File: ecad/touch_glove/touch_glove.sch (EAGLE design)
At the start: 175 parts, among them Q1 MCH3474 4A/30V, Q2 MCH3474 4A/30V, Q3 MCH3474 4A/30V, Q4 MCH3474 4A/30V, Q5 MCH3474 4A/30V, Q6 MCH3474 4A/30V, SW1 4A/28V

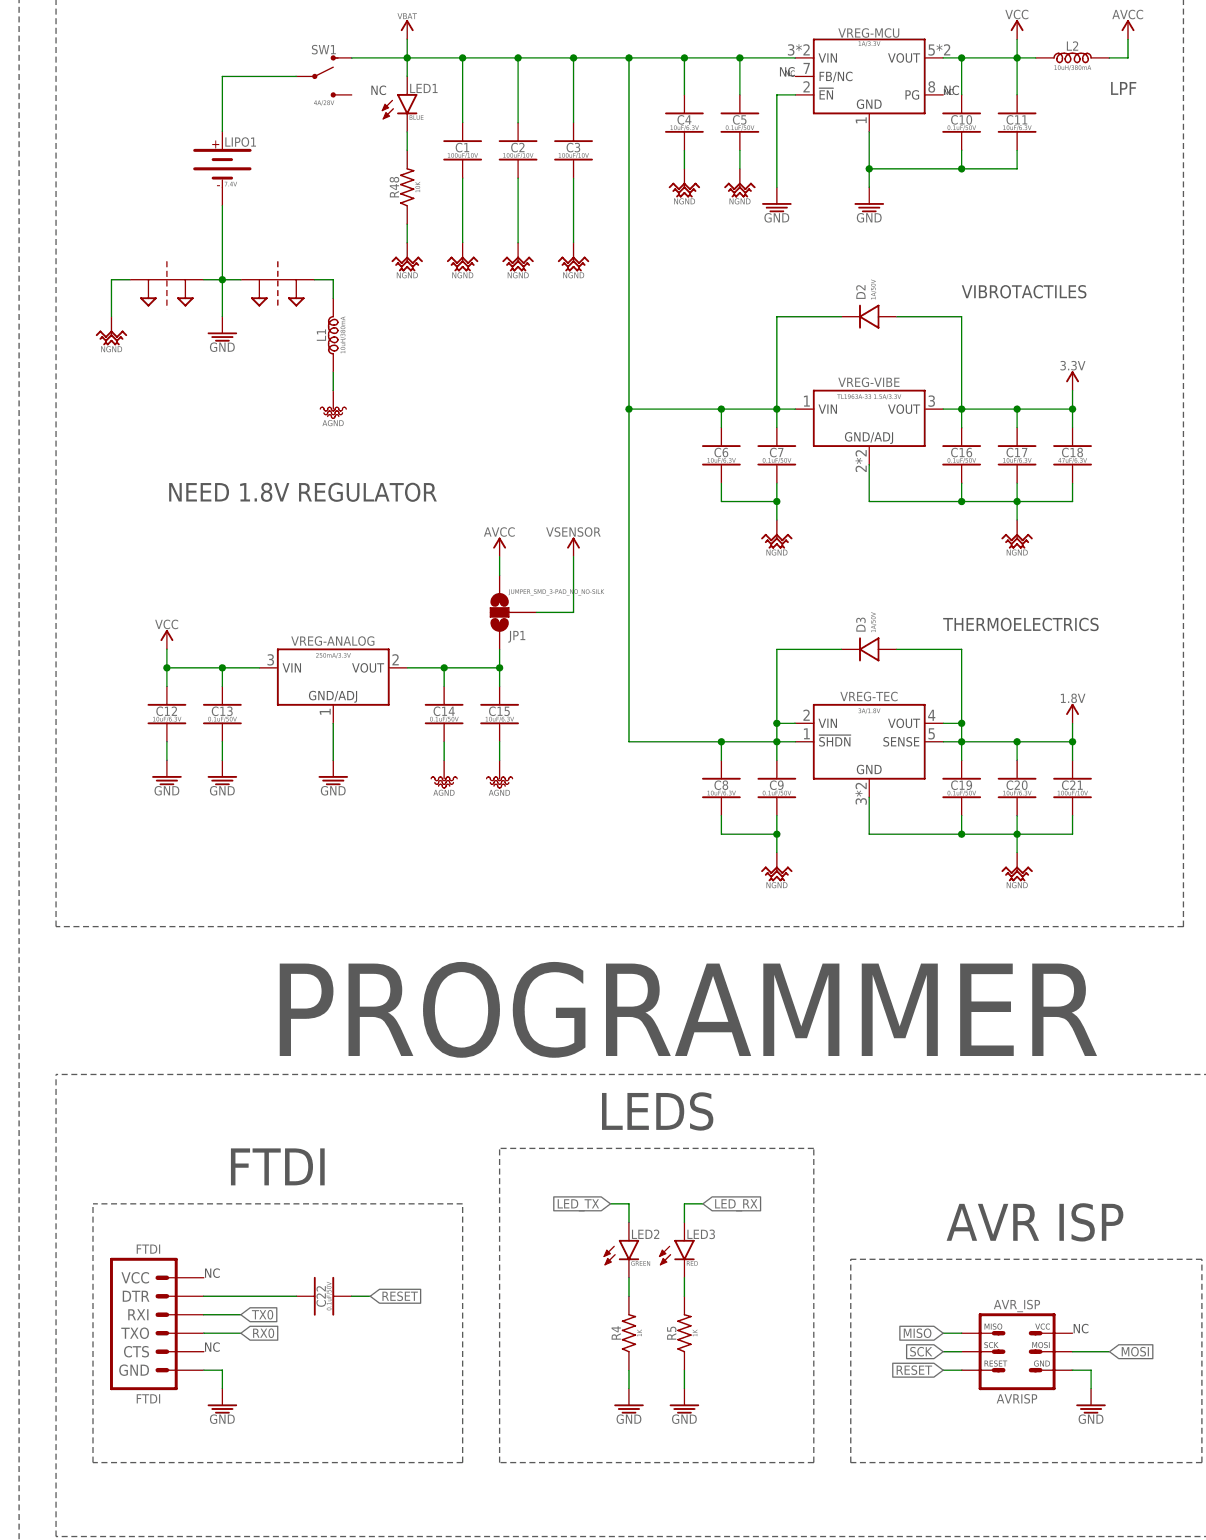
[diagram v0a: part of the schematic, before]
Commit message: Massive updates to code.  Changed touch glove PCB to Rev 3 with 1.8V regulator, confirmed to work.
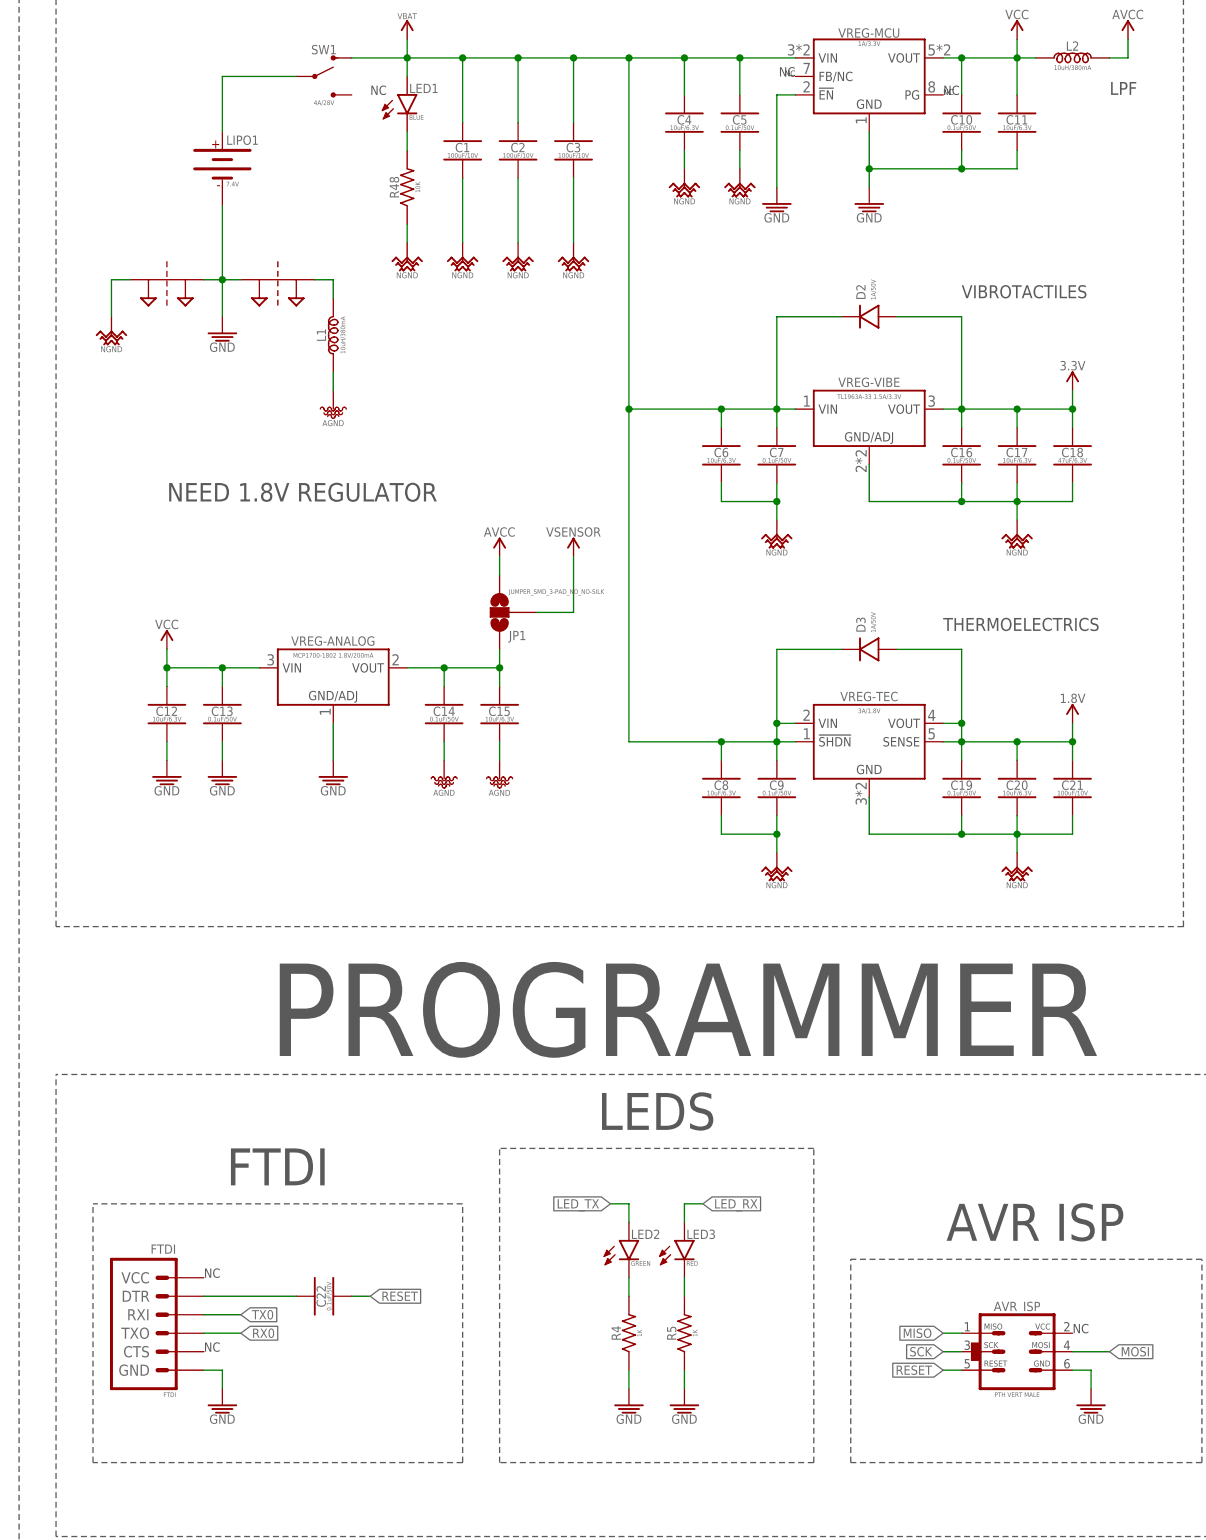
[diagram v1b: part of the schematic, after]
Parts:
- AVR_ISP: value AVRISP -> PTH VERT MALE; device PiB_connectors:AVR_SPI_PRG_6_PTH_VERT-MALE -> PiB_connectors:AVR_SPI_PRG_6_PTH_VERT_MALE_2.54MM
- VREG-ANALOG: value 250mA/3.3V -> MCP1700-1802 1.8V/200mA; device PiB_ic_power:VREG_LINEAR_MCP1700_SOT-23_ -> PiB_ic_power:VREG_LINEAR_MCP1700_MCP1700T-1802_1.8V-200MA_SOT-23
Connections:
- net N$39 renamed AREF
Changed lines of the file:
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@@
 <part name="GND125" library="PiB_power_symbols" deviceset="GND" device=""/>
 <part name="SUPPLY84" library="PiB_power_symbols" deviceset="VCC" device=""/>
-<part name="AVR_ISP" library="PiB_connectors" deviceset="AVR_SPI_PRG_6" device="_PTH_VERT-MALE" package3d_urn="urn:adsk.eagle:package:2993074/7" value="AVRISP"/>
+<part name="AVR_ISP" library="PiB_connectors" deviceset="AVR_SPI_PRG_6" device="_PTH_VERT_MALE_2.54MM" package3d_urn="urn:adsk.eagle:package:4860635/1" value="PTH VERT MALE"/>
 <part name="C22" library="PiB_capacitors" deviceset="0.1UF" device="_SMD-0402_50V-10%" package3d_urn="urn:adsk.eagle:package:2886515/1" value="0.1uF/50V"/>
 <part name="FTDI" library="PiB_connectors" deviceset="FTDI" device="_PTH_RA-MALE" package3d_urn="urn:adsk.eagle:package:2993075/7" value="FTDI"/>
@@
 <part name="SUPPLY57" library="PiB_power_symbols" deviceset="AGND" device=""/>
 <part name="SUPPLY58" library="PiB_power_symbols" deviceset="VCC" device=""/>
-<part name="VREG-ANALOG" library="PiB_ic_power" deviceset="VREG_LINEAR_MCP1700" device="_SOT-23_" package3d_urn="urn:adsk.eagle:package:2889826/1" value="250mA/3.3V"/>
+<part name="VREG-ANALOG" library="PiB_ic_power" deviceset="VREG_LINEAR_MCP1700" device="_MCP1700T-1802_1.8V-200MA_SOT-23" package3d_urn="urn:adsk.eagle:package:2889826/1" value="MCP1700-1802 1.8V/200mA"/>
 <part name="SUPPLY100" library="PiB_power_symbols" deviceset="GND" device=""/>
 <part name="SUPPLY101" library="PiB_power_symbols" deviceset="GND" device=""/>
@@
 </segment>
 </net>
-<net name="N$39" class="0">
+<net name="AREF" class="0">
 <segment>
 <pinref part="JP2" gate="G$1" pin="2"/>

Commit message: Start on Rev 2 of robotic arm.  Made minor fixes to Touch Glove Rev 2.
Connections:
- net N$33 renamed A1.8V
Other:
- note removed: "NEED 1.8V REGULATOR"
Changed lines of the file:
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@@
 <part name="SUPPLY123" library="PiB_power_symbols" deviceset="VSENSOR" device=""/>
 <part name="SUPPLY83" library="PiB_power_symbols" deviceset="VCC" device=""/>
+<part name="SUPPLY124" library="PiB_power_symbols" deviceset="A1.8V" device=""/>
 </parts>
 <sheets>
@@
 <text x="365.76" y="96.52" size="1.27" layer="97" font="vector" ratio="10">NC</text>
 <text x="246.38" y="104.14" size="1.27" layer="97" font="vector" ratio="10">NC</text>
-<text x="241.3" y="210.82" size="2.54" layer="97" font="vector" ratio="10">NEED 1.8V REGULATOR</text>
 <wire x1="287.02" y1="78.74" x2="287.02" y2="121.92" width="0.1524" layer="97" style="shortdash"/>
 <wire x1="330.2" y1="121.92" x2="287.02" y2="121.92" width="0.1524" layer="97" style="shortdash"/>
@@
 <instance part="SUPPLY123" gate="G$1" x="546.1" y="223.52"/>
 <instance part="SUPPLY83" gate="VCC" x="299.72" y="449.58"/>
+<instance part="SUPPLY124" gate="G$1" x="279.4" y="190.5"/>
 </instances>
 <busses>
@@
 <wire x1="264.16" y1="238.76" x2="264.16" y2="241.3" width="0.1524" layer="91"/>
 <wire x1="264.16" y1="241.3" x2="261.62" y2="241.3" width="0.1524" layer="91"/>
-</segment>
-</net>
-<net name="N$33" class="3">
-<segment>
-<wire x1="287.02" y1="187.96" x2="279.4" y2="187.96" width="0.1524" layer="91"/>
-<pinref part="C15" gate="G$1" pin="1"/>
-<wire x1="279.4" y1="187.96" x2="274.32" y2="187.96" width="0.1524" layer="91"/>
-<wire x1="287.02" y1="185.42" x2="287.02" y2="187.96" width="0.1524" layer="91"/>
-<pinref part="C14" gate="G$1" pin="1"/>
-<wire x1="279.4" y1="185.42" x2="279.4" y2="187.96" width="0.1524" layer="91"/>
-<junction x="279.4" y="187.96"/>
-<pinref part="VREG-ANALOG" gate="G$1" pin="VO"/>
-<pinref part="JP1" gate="G$1" pin="1"/>
-<wire x1="287.02" y1="190.5" x2="287.02" y2="187.96" width="0.1524" layer="91"/>
-<junction x="287.02" y="187.96"/>
 </segment>
 </net>
@@
 </segment>
 </net>
+<net name="A1.8V" class="0">
+<segment>
+<wire x1="287.02" y1="187.96" x2="279.4" y2="187.96" width="0.1524" layer="91"/>
+<pinref part="C15" gate="G$1" pin="1"/>
+<wire x1="279.4" y1="187.96" x2="274.32" y2="187.96" width="0.1524" layer="91"/>
+<wire x1="287.02" y1="185.42" x2="287.02" y2="187.96" width="0.1524" layer="91"/>
+<pinref part="C14" gate="G$1" pin="1"/>
+<wire x1="279.4" y1="185.42" x2="279.4" y2="187.96" width="0.1524" layer="91"/>
+<junction x="279.4" y="187.96"/>
+<pinref part="VREG-ANALOG" gate="G$1" pin="VO"/>
+<pinref part="JP1" gate="G$1" pin="1"/>
+<wire x1="287.02" y1="190.5" x2="287.02" y2="187.96" width="0.1524" layer="91"/>
+<junction x="287.02" y="187.96"/>
+<pinref part="SUPPLY124" gate="G$1" pin="A1.8V"/>
+<wire x1="279.4" y1="190.5" x2="279.4" y2="187.96" width="0.1524" layer="91"/>
+</segment>
+</net>

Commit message: Rev 3: Changes to robotic and and touch glove to fix inconsistencies and errors from Rev 2.
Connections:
- net N$15: now also VIBE-RING.-; no longer VIBE-PINKY.-
- net N$17: now also VIBE-PINKY.-; no longer VIBE-PALM.-
- net N$2: now also VIBE-INDEX.-; no longer VIBE-MIDDLE.-
- net N$3: now also VIBE-THUMB.-; no longer VIBE-INDEX.-
- net N$30: now also VIBE-PALM.-; no longer VIBE-THUMB.-
- net N$4: now also VIBE-MIDDLE.-; no longer VIBE-RING.-
- net VIBE-INDEX: now also PWM_DRIVER1.PWM3, R19.1; no longer PWM_DRIVER1.PWM4, R20.1
- net VIBE-MIDDLE: now also PWM_DRIVER1.PWM2, R18.1; no longer PWM_DRIVER1.PWM3, R19.1
- net VIBE-PALM: now also PWM_DRIVER1.PWM5, R21.1; no longer PWM_DRIVER1.PWM0, R16.1
- net VIBE-PINKY: now also PWM_DRIVER1.PWM0, R16.1; no longer PWM_DRIVER1.PWM1, R17.1
- net VIBE-RING: now also PWM_DRIVER1.PWM1, R17.1; no longer PWM_DRIVER1.PWM2, R18.1
- net VIBE-THUMB: now also PWM_DRIVER1.PWM4, R20.1; no longer PWM_DRIVER1.PWM5, R21.1
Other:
- moved on the sheet: D10, D5, D6, D7, D8, D9, Q1, Q2, Q3, Q4, Q5, Q6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

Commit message: Update all components to new libraries.
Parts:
- removed C37, C49: 10uF/6.3V, PiB_capacitors:10UF_CER_SMD-0402_6.3V-20%
- ANT: device PiB_radio_frequency:ANTENNA_SMD_CHP-2.45GHZ-0.5DBI-3W -> _radio_frequency:ANTENNA_SMD_CHP-2.45GHZ-0.5DBI-3W
- AVR_ISP: device PiB_connectors:AVR_SPI_PRG_6_PTH_VERT_MALE_2.54MM -> _connectors:AVR_SPI_PRG_6_PTH_VERT_MALE_2.54MM
- BALUN1: device PiB_radio_frequency:BALUN_SMD-0805_UNBAL/BAL-50/100 -> _radio_frequency:BALUN_SMD-0805_UNBAL/BAL-50/100
- BR_ANALOG, BR_NOISE: value 2PT_GND_TIE -> NET_BRIDGE; device PiB_power_symbols:2PT_GND_TIE -> _power_symbols:NET_BRIDGE
- C1, C2, C21, C3: device PiB_capacitors:100UF_CER_SMD-1210_16V-20% -> _capacitors:100UF-POLARIZED_TANT_SMD-1206_10V-20%
- C10, C13, C14, C16, C19, C22, C23, C25, C27, C30, C38, C39, C40, C41, C42, C43, C44, C45, C46, C47, C48, C5, C50, C51, C52, C53, C54, C55, C56, C57, C58, C59, C60, C7, C9: device PiB_capacitors:0.1UF_SMD-0402_50V-10% -> _capacitors:0.1UF_SMD-0402_50V-10%
- C11, C12, C15, C17, C20, C4, C6, C8: device PiB_capacitors:10UF_CER_SMD-0402_6.3V-20% -> _capacitors:10UF_CER_SMD-0402_6.3V-20%
- C18: value 47uF/6.3V -> 100uF/10V; device PiB_capacitors:47UF_SMD-0805_6.3V-20% -> _capacitors:100UF-POLARIZED_TANT_SMD-1206_10V-20%
- C24, C26, C28, C29, C31, C32: device PiB_capacitors:1UF_CER_SMD-0402_25V-10% -> _capacitors:1UF_CER_SMD-0402_25V-10%
- C33, C34: device PiB_capacitors:12PF_SMD-0402_100V-5% -> _capacitors:12PF_SMD-0402_100V-5%
- C35: device PiB_capacitors:0.75PF_CER_SMD-0402_50V-33% -> _capacitors:0.75PF_CER_SMD-0402_50V-33%
- C36: device PiB_capacitors:22PF_CER_SMD-0402-100V-5% -> _capacitors:22PF_CER_SMD-0402-100V-5%
- D10, D4, D5, D6, D7, D8, D9: device PiB_discrete_semiconductors:DIODE_GENERAL-PURPOSE_SMD-0402_GP_150MA-75V -> _discrete_semiconductors:GENERAL-PURPOSE_SMD-0402_GP_150MA-75V
- D2, D3: device PiB_discrete_semiconductors:DIODE_GENERAL-PURPOSE_SMD_GP_1A-50V -> _discrete_semiconductors:GENERAL-PURPOSE_SMD_GP_1A-50V
- DEMUX1: device PiB:CD74HC4067-SM96_16:1_MUX-DEMUX_SOP-24_16:1-MUX-DEMUX -> _special:CD74HC4067-SM96_16:1_MUX-DEMUX_SOP-24_16:1-MUX-DEMUX
- FLEX-INDEX, FLEX-MIDDLE, FLEX-PINKY, FLEX-RING, FLEX-THUMB: device PiB_sensors:FLEX-SENSOR_0530480210_RA-MALE_PITCH-1.25MM -> _sensors:FLEX_SENSOR_0530470210_VERT-MALE_PITCH-1.25MM
- FLEX-INDEX2, FLEX-MIDDLE2, FLEX-PINKY2, FLEX-RING2, FLEX-THUMB2: device PiB_sensors:FLEX-SENSOR_0530470210_VERT-MALE_PITCH-1.25MM -> _sensors:FLEX_SENSOR_0530470210_VERT-MALE_PITCH-1.25MM
- FTDI: device PiB_connectors:FTDI_PTH_RA-MALE -> _connectors:FTDI_PTH_RA-MALE
- HBRIDGE-INDEX, HBRIDGE-MIDDLE, HBRIDGE-PINKY, HBRIDGE-RING, HBRIDGE-THUMB: device PiB:DRV883X_H-BRIDGE_DRV8837C_1A -> _special:DRV883X_H-BRIDGE_DRV8837C_1A
- JP1: value JUMPER_SMD_3-PAD_NO_NO-SILK -> JUMPER_SMD_3-PAD_NO_SILK; device PiB_connectors:JUMPER_SMD_3-PAD_NO_NO-SILK -> _connectors:JUMPER_SMD_3-PAD_NO_SILK
- JP2: device PiB_connectors:JUMPER_SMD_2-PAD_NO_SILK -> _connectors:JUMPER_SMD_2-PAD_NO_SILK
- L1, L2: device PiB_inductors:10UH_SMD-0603_0.38A-0.468OHM-10% -> _inductors:10UH_SMD-0603_0.38A-0.468OHM-10%
- LED1: device PiB_leds:LED_SMD-0402_DISCRETE_BLUE -> _leds:LED_SMD-0402_DISCRETE_BLUE
- LED2: device PiB_leds:LED_SMD-0402_DISCRETE_GREEN -> _leds:LED_SMD-0402_DISCRETE_GREEN
- LED3: device PiB_leds:LED_SMD-0402_DISCRETE_RED -> _leds:LED_SMD-0402_DISCRETE_RED
- LIPO1: device PiB_batteries:BATTERY-CONNECTOR_MOLEX_89401_RA-MALE_PITCH-2MM -> _batteries:BATTERY-CONNECTOR_MOLEX_0530470210_VERT-MALE_PITCH-1.25MM
- MCU: device PiB_ic_microcontrollers:ATMEGA128RFA1_VFQFN-64_EXPOSED-PAD -> _ic_microcontrollers:ATMEGA128RFA1_VFQFN-64_EXPOSED-PAD
- OPAMP1, OPAMP2, OPAMP3: device PiB_op_amps:LM358_DFN-EP -> _op_amps:LM358_DFN-EP
- PWM_DRIVER1: device PiB:PCA9685_16-CH_12-BIT_PWM-DRIVER_TSSOP-28_PWM-DRIVER_16CH -> _special:PCA9685_16-CH_12-BIT_PWM-DRIVER_TSSOP-28_PWM-DRIVER_16CH
- Q1, Q2, Q3, Q4, Q5, Q6: device PiB_discrete_semiconductors:POWER_NCHAN_MCH3474_NMOS_4A-30V -> _transistors:POWER_NCHAN_MCH3474_NMOS_4A-30V
- R1, R10, R11, R12, R13, R14, R15, R32, R33, R34, R35, R36, R37, R38, R39, R40, R41, R42, R43, R44, R45, R46, R47, R48, R6, R7, R8, R9: device PiB_resistors:10KΩ_SMD-0402_1/16W-5% -> _resistors:10KΩ_SMD-0402_1/16W-5%
- R16, R17, R18, R19, R20, R21, R22, R23, R24, R25, R26, R27, R28, R29, R30, R31: device PiB_resistors:100Ω_SMD-0402_1/16W-5% -> _resistors:100Ω_SMD-0402_1/16W-5%
- R2, R3: device PiB_resistors:4.7KΩ_SMD-0402_1/16W-5% -> _resistors:4.7KΩ_SMD-0402_1/16W-5%
- R4, R5: device PiB_resistors:1KΩ_SMD-0402_1/16W-5% -> _resistors:1KΩ_SMD-0402_1/16W-5%
- SW1: device PiB_switches:SWITCH_SPDT_RA_PTH_4A-28V_L12.7-W9.5 -> _switches:SWITCH_SPDT_RA_PTH_4A-28V_L12.7-W9.5
- TEC-INDEX, TEC-MIDDLE, TEC-PINKY, TEC-RING, TEC-THUMB: value Molex RA 1.25mm pitch -> PELTIER; device PiB_actuators:PELTIER-TEC_CONNECTOR_0530480210_RA-MALE_PITCH-1.25MM -> _actuators:PELTIER-TEC_CONNECTOR_0530470210_VERT-MALE_PITCH-1.25MM
- VIBE-INDEX, VIBE-MIDDLE, VIBE-PALM, VIBE-PINKY, VIBE-RING, VIBE-THUMB: value Molex RA 1.25mm pitch -> Molex VERT 1.25mm pitch; device PiB_actuators:VIBE-MOTOR_CONNECTOR_0530480210_RA-MALE_PITCH-1.25MM -> _actuators:VIBE-MOTOR_CONNECTOR_0530470210_VERT-MALE_PITCH-1.25MM
- VREG-ANALOG: device PiB_ic_power:VREG_LINEAR_MCP1700_MCP1700T-1802_1.8V-200MA_SOT-23 -> _ic_power:VREG_LINEAR_MCP1700_MCP1700T-1802_1.8V-200MA_SOT-23
- VREG-MCU: value 1A/3.3V -> TPS76833QDR 1A/3.3V; device PiB_ic_power:VREG_TPS768XX_ULDO_FAST-TRANSIENT_TPS76833QDR_1A-3.3V -> _ic_power:VREG_TPS768XX_ULDO_FAST-TRANSIENT_TPS76833QDR_1A-3.3V
- VREG-TEC: device PiB_ic_power:VREG_LT1764EQ_ULDO_FAST-TRANSIENT_LT1764EQ-1.8_3A_1.8V -> _ic_power:VREG_LT1764EQ_ULDO_FAST-TRANSIENT_LT1764EQ-1.8_3A_1.8V
- VREG-VIBE: device PiB_ic_power:VREG_TL1963A-XX_1.5A_LN_LDO_FAST-TRANSIENT_SOT-223-4_TL1963A-33_1.5A-3.3V -> _ic_power:VREG_TL1963A-XX_1.5A_LN_LDO_FAST-TRANSIENT_SOT-223-4_TL1963A-33_1.5A-3.3V
- XTAL: device PiB:CRYSTAL_ABM3B_16MHZ_18PF -> _crystals_oscillators_resonators:CRYSTAL_ABM3B_16MHZ_18PF
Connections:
- net 1.8V: now also C21.A; no longer C21.1
- net 3.3V: now also C18.A; no longer C18.1
- net AGND: no longer C37.2
- net FLEX-INDEX2: now also OPAMP1.OUT-A; no longer OPAMP1.OUT-A+
- net FLEX-PINKY2: now also OPAMP3.OUT-A; no longer OPAMP3.OUT-A+
- net FLEX-RING2: now also OPAMP2.OUT-A; no longer OPAMP2.OUT-A+
- net GND: no longer C49.2
- net NGND: now also C1.K, C18.K, C2.K, C21.K, C3.K; no longer C1.2, C18.2, C2.2, C21.2, C3.2
- net VBAT: now also C1.A, C2.A, C3.A; no longer C1.1, C2.1, C3.1
- net VCC: no longer C49.1
- net VSENSOR: no longer C37.1

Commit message: Fix all errors on board.
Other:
- note added: "Rev 3"
- note removed: "Rev 2"
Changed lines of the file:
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@@
 <text x="264.16" y="548.64" size="20.32" layer="97" font="vector" ratio="20" align="bottom-center">TRANSMISSION OF TOUCH VR</text>
 <text x="264.16" y="528.32" size="12.7" layer="97" font="vector" ratio="20" align="bottom-center">TOUCH GLOVE</text>
-<text x="264.16" y="515.62" size="8.128" layer="97" font="vector" ratio="20" align="bottom-center">Rev 2</text>
+<text x="264.16" y="515.62" size="8.128" layer="97" font="vector" ratio="20" align="bottom-center">Rev 3</text>
 <text x="350.52" y="238.76" size="1.778" layer="97">VIBROTACTILES</text>
 <text x="347.98" y="193.04" size="1.778" layer="97">THERMOELECTRICS</text>
